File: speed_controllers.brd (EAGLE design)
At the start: 147.3 x 147.3 mm, 9 parts

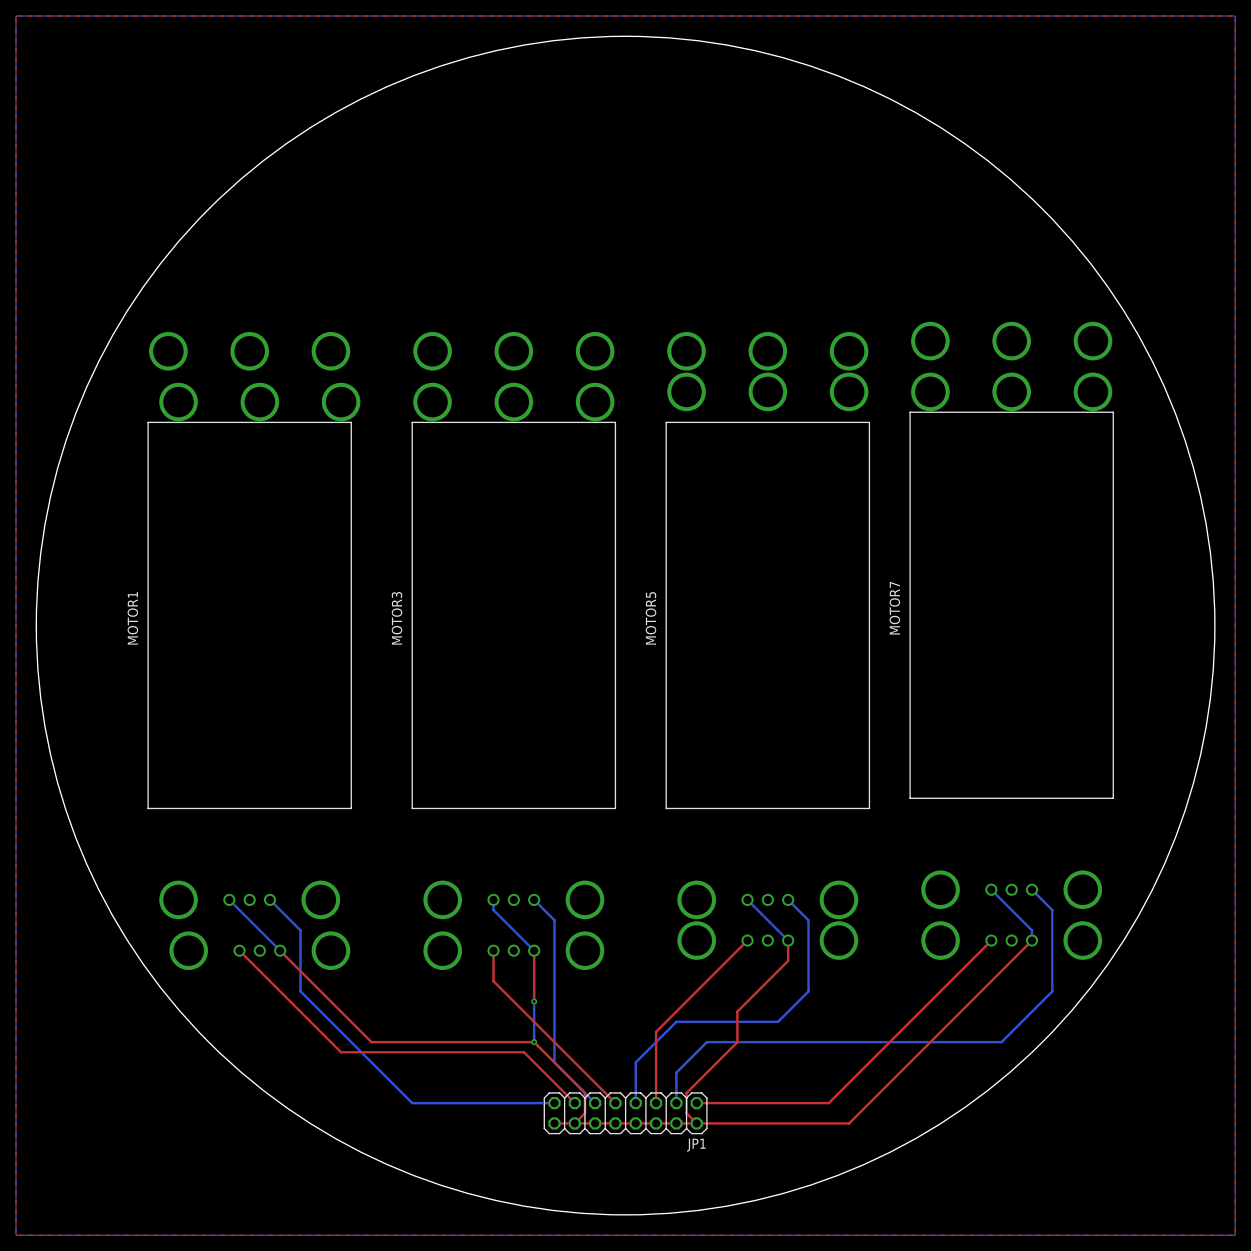
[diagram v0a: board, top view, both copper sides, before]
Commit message: Added MOSFETs to speed controllers
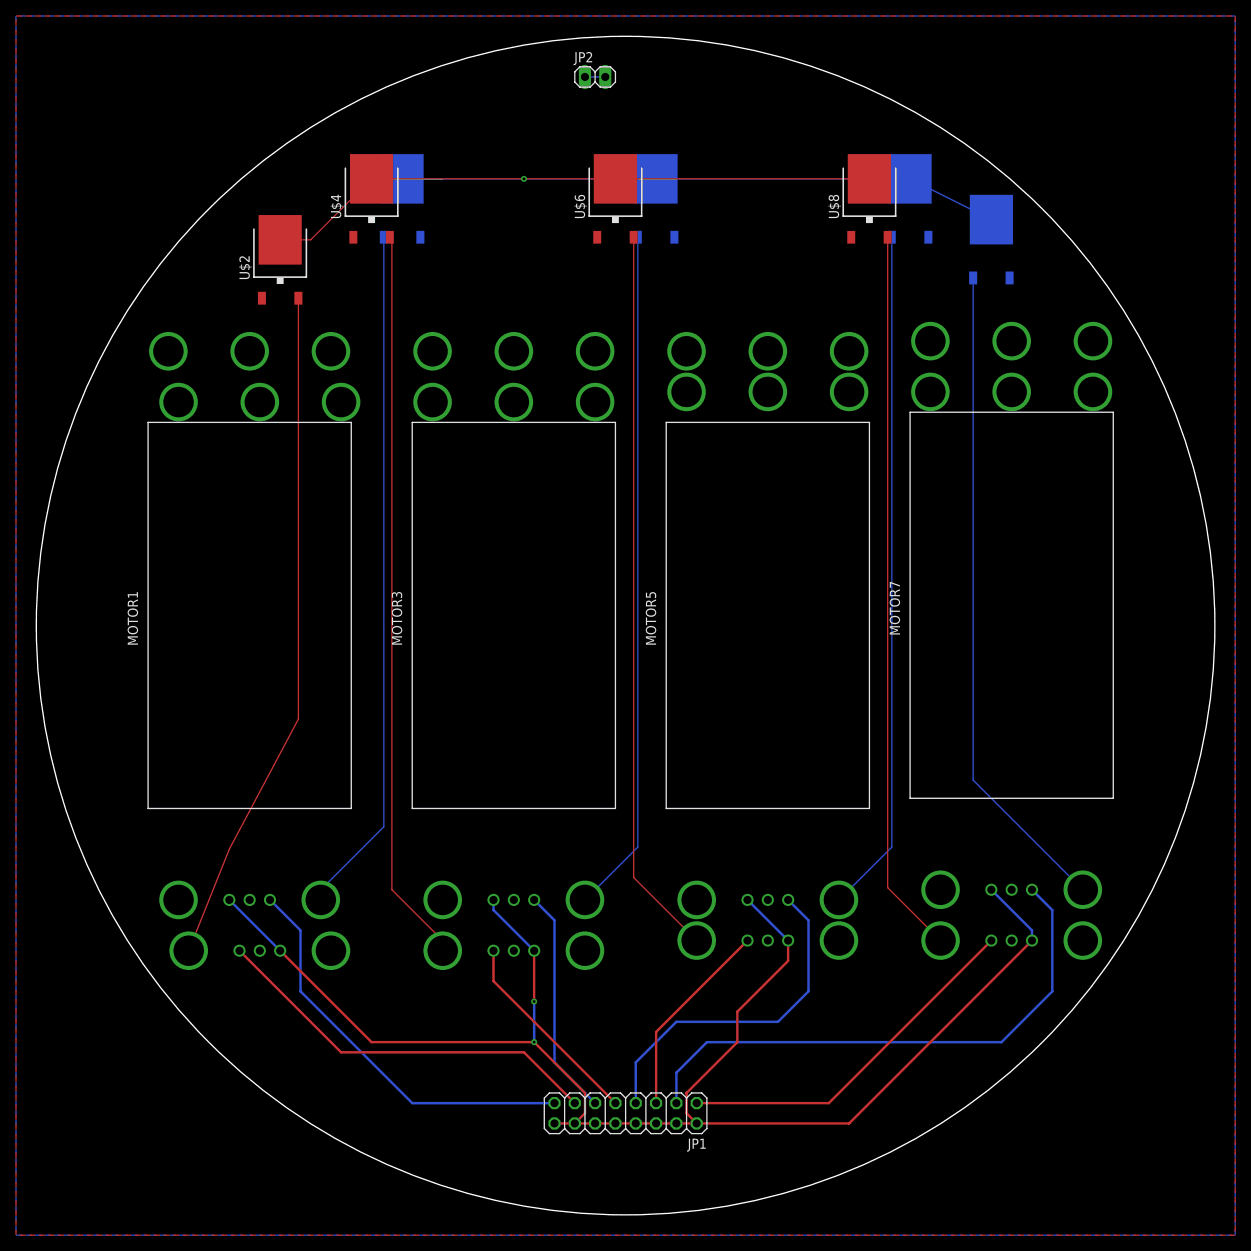
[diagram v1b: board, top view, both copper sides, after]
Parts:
- added JP2: (no value), auv:1X02
- added U$1, U$2, U$3, U$4, U$5, U$6, U$7, U$8: AOD403, auv:TO252
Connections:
- new net N$10: MOTOR1.VIN, U$1.2
- new net N$11: MOTOR2.VIN, U$2.2
- new net N$12: MOTOR3.VIN, U$3.2
- new net N$13: MOTOR4.VIN, U$4.2
- new net N$14: MOTOR7.VIN, U$7.2
- new net N$15: MOTOR6.VIN, U$6.2
- new net N$16: MOTOR8.VIN, U$8.2
- new net N$17: JP2.1, JP2.2
- new net N$19: MOTOR5.VIN, U$5.2
- net VCC: now also U$1.3, U$2.3, U$3.3, U$4.3, U$5.3, U$6.3, U$7.3, U$8.3; no longer MOTOR1.VIN, MOTOR2.VIN, MOTOR3.VIN, MOTOR4.VIN, MOTOR5.VIN, MOTOR6.VIN, MOTOR7.VIN, MOTOR8.VIN
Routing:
- net VCC: track 0.00 -> 158.0 mm, vias 0 -> 1
- net N$13: track 0.00 -> 91.9 mm
- net N$15: track 0.00 -> 91.2 mm
- net N$16: track 0.00 -> 90.6 mm
- net N$10: track 0.00 -> 86.1 mm
- net N$19: track 0.00 -> 85.6 mm
- net N$12: track 0.00 -> 85.6 mm
- net N$11: track 0.00 -> 84.7 mm
- net N$14: track 0.00 -> 82.2 mm
- net N$17: track 0.00 -> 2.54 mm
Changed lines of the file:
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@@
 <?xml version="1.0" encoding="utf-8"?>
 <!DOCTYPE eagle SYSTEM "eagle.dtd">
-<eagle version="8.4.1">
+<eagle version="8.4.3">
 <drawing>
 <settings>
@@
 <element name="MOTOR7" library="auv" package="ESC" value="ESC" x="48.26" y="3.81"/>
 <element name="MOTOR8" library="auv" package="ESC" value="ESC" x="48.26" y="-2.54" rot="MR0"/>
+<element name="U$1" library="auv" package="TO252" value="AOD403" x="-27.94" y="53.34" rot="MR0"/>
+<element name="U$2" library="auv" package="TO252" value="AOD403" x="-43.18" y="45.72"/>
+<element name="U$3" library="auv" package="TO252" value="AOD403" x="3.81" y="53.34" rot="MR0"/>
+<element name="U$4" library="auv" package="TO252" value="AOD403" x="-31.75" y="53.34"/>
+<element name="U$5" library="auv" package="TO252" value="AOD403" x="35.56" y="53.34" rot="MR0"/>
+<element name="U$6" library="auv" package="TO252" value="AOD403" x="-1.27" y="53.34"/>
+<element name="U$7" library="auv" package="TO252" value="AOD403" x="45.72" y="48.26" rot="MR0"/>
+<element name="U$8" library="auv" package="TO252" value="AOD403" x="30.48" y="53.34"/>
+<element name="JP2" library="auv" package="1X02" value="" x="-3.81" y="68.58"/>
 </elements>
 <signals>
@@
 </signal>
 <signal name="VCC">
-<contactref element="MOTOR1" pad="VIN"/>
-<contactref element="MOTOR2" pad="VIN"/>
-<contactref element="MOTOR3" pad="VIN"/>
-<contactref element="MOTOR8" pad="VIN"/>
-<contactref element="MOTOR7" pad="VIN"/>
-<contactref element="MOTOR4" pad="VIN"/>
-<contactref element="MOTOR5" pad="VIN"/>
-<contactref element="MOTOR6" pad="VIN"/>
 <polygon width="0.4064" layer="1" isolate="0.254" thermals="no">
 <vertex x="-76.2" y="76.2"/>
@@
 <vertex x="-76.2" y="-76.2"/>
 </polygon>
+<contactref element="U$1" pad="3"/>
+<contactref element="U$2" pad="3"/>
+<contactref element="U$3" pad="3"/>
+<contactref element="U$4" pad="3"/>
+<contactref element="U$6" pad="3"/>
+<contactref element="U$7" pad="3"/>
+<contactref element="U$8" pad="3"/>
+<contactref element="U$5" pad="3"/>
+<wire x1="45.72" y1="50.76" x2="35.56" y2="55.84" width="0.1524" layer="16"/>
+<wire x1="-22.86" y1="55.88" x2="-22.9" y2="55.84" width="0.1524" layer="16"/>
+<wire x1="-27.94" y1="55.84" x2="-22.9" y2="55.84" width="0.1524" layer="16"/>
+<wire x1="3.81" y1="54.61" x2="3.81" y2="55.84" width="0.1524" layer="16"/>
+<wire x1="35.56" y1="55.84" x2="3.81" y2="55.84" width="0.1524" layer="16"/>
+<wire x1="3.81" y1="55.84" x2="-12.7" y2="55.84" width="0.1524" layer="16"/>
+<wire x1="-12.7" y1="55.84" x2="-27.94" y2="55.84" width="0.1524" layer="16"/>
+<wire x1="30.48" y1="55.84" x2="-1.27" y2="55.84" width="0.1524" layer="1"/>
+<wire x1="-43.18" y1="48.22" x2="-39.37" y2="48.22" width="0.1524" layer="1"/>
+<wire x1="-31.75" y1="55.84" x2="-39.37" y2="48.22" width="0.1524" layer="1"/>
+<wire x1="-1.27" y1="55.84" x2="-12.7" y2="55.84" width="0.1524" layer="1"/>
+<wire x1="-12.7" y1="55.84" x2="-31.75" y2="55.84" width="0.1524" layer="1"/>
+<via x="-12.7" y="55.84" extent="1-16" drill="0.35"/>
 </signal>
 <signal name="N$1">
@@
 <wire x1="6.35" y1="-62.23" x2="8.89" y2="-62.23" width="0.3048" layer="1"/>
 </signal>
+<signal name="N$10">
+<contactref element="U$1" pad="2"/>
+<contactref element="MOTOR1" pad="VIN"/>
+<wire x1="-30.22" y1="48.54" x2="-30.22" y2="-25.14" width="0.1524" layer="16"/>
+<wire x1="-30.22" y1="-25.14" x2="-38.1" y2="-33.02" width="0.1524" layer="16"/>
+<wire x1="-38.1" y1="-33.02" x2="-38.1" y2="-34.29" width="0.1524" layer="16"/>
+</signal>
+<signal name="N$11">
+<contactref element="U$2" pad="2"/>
+<contactref element="MOTOR2" pad="VIN"/>
+<wire x1="-40.9" y1="40.92" x2="-40.9" y2="-11.69" width="0.1524" layer="1"/>
+<wire x1="-40.9" y1="-11.69" x2="-49.53" y2="-27.94" width="0.1524" layer="1"/>
+<wire x1="-49.53" y1="-27.94" x2="-54.61" y2="-40.64" width="0.1524" layer="1"/>
+</signal>
+<signal name="N$12">
+<contactref element="MOTOR3" pad="VIN"/>
+<contactref element="U$3" pad="2"/>
+<wire x1="1.53" y1="48.54" x2="1.53" y2="-27.68" width="0.1524" layer="16"/>
+<wire x1="1.53" y1="-27.68" x2="-5.08" y2="-34.29" width="0.1524" layer="16"/>
+</signal>
+<signal name="N$13">
+<contactref element="MOTOR4" pad="VIN"/>
+<contactref element="U$4" pad="2"/>
+<wire x1="-29.47" y1="48.54" x2="-29.21" y2="48.28" width="0.1524" layer="1"/>
+<wire x1="-29.21" y1="48.28" x2="-29.21" y2="-33.02" width="0.1524" layer="1"/>
+<wire x1="-29.21" y1="-33.02" x2="-22.86" y2="-39.37" width="0.1524" layer="1"/>
+<wire x1="-22.86" y1="-39.37" x2="-22.86" y2="-40.64" width="0.1524" layer="1"/>
+</signal>
+<signal name="N$15">
+<contactref element="MOTOR6" pad="VIN"/>
+<contactref element="U$6" pad="2"/>
+<wire x1="1.01" y1="48.54" x2="1.01" y2="-31.49" width="0.1524" layer="1"/>
+<wire x1="1.01" y1="-31.49" x2="8.89" y2="-39.37" width="0.1524" layer="1"/>
+</signal>
+<signal name="N$14">
+<contactref element="MOTOR7" pad="VIN"/>
+<contactref element="U$7" pad="2"/>
+<wire x1="43.44" y1="43.46" x2="43.44" y2="-19.31" width="0.1524" layer="16"/>
+<wire x1="43.44" y1="-19.31" x2="57.15" y2="-33.02" width="0.1524" layer="16"/>
+</signal>
+<signal name="N$16">
+<contactref element="U$8" pad="2"/>
+<contactref element="MOTOR8" pad="VIN"/>
+<wire x1="32.76" y1="48.54" x2="32.76" y2="-32.76" width="0.1524" layer="1"/>
+<wire x1="32.76" y1="-32.76" x2="39.37" y2="-39.37" width="0.1524" layer="1"/>
+</signal>
+<signal name="N$17">
+<contactref element="JP2" pad="1"/>
+<contactref element="JP2" pad="2"/>
+<wire x1="-2.54" y1="68.58" x2="-5.08" y2="68.58" width="0.1524" layer="16"/>
+</signal>
+<signal name="N$19">
+<contactref element="MOTOR5" pad="VIN"/>
+<contactref element="U$5" pad="2"/>
+<wire x1="33.28" y1="48.54" x2="33.28" y2="-27.68" width="0.1524" layer="16"/>
+<wire x1="33.28" y1="-27.68" x2="26.67" y2="-34.29" width="0.1524" layer="16"/>
+</signal>
 </signals>
